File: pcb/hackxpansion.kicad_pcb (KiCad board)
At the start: 2 copper layers, 30 parts, among them J1 Conn_01x03_MountingPin, SW1 SW_Push, SW2 SW_Push, U1 ADS131M08xPBS, U2 RP2354B, Y1 ABM8-272-T3

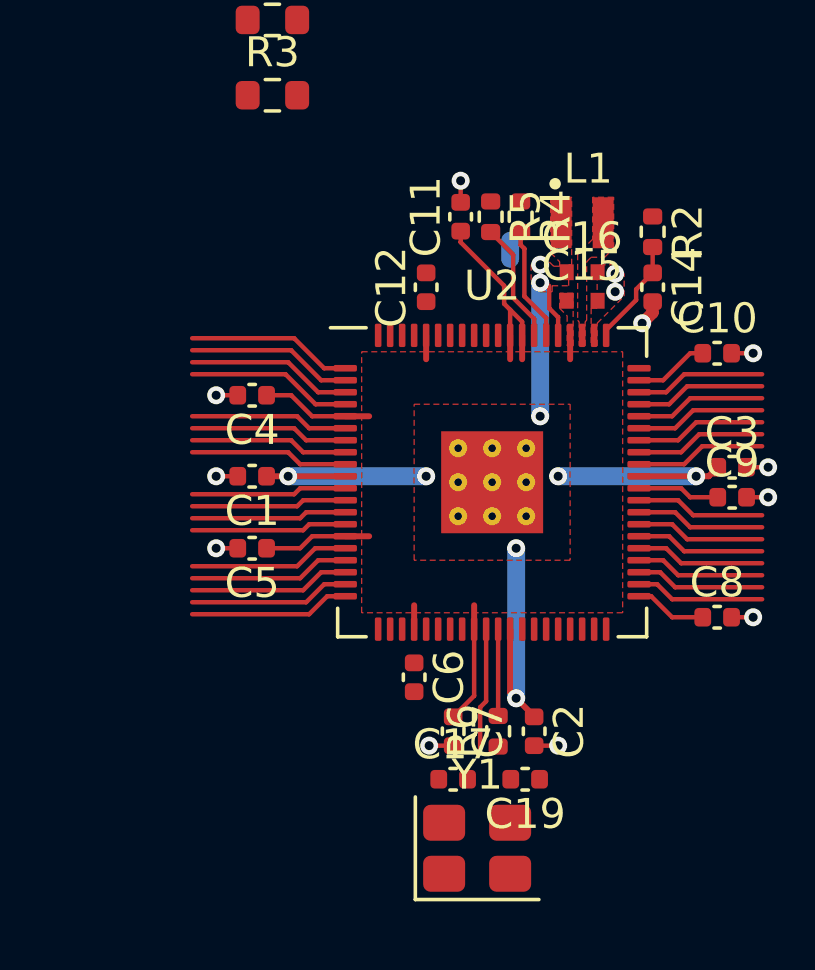
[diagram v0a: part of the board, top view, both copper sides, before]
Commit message: More fanout
Just a little bit further with the fanout of the RP2354B
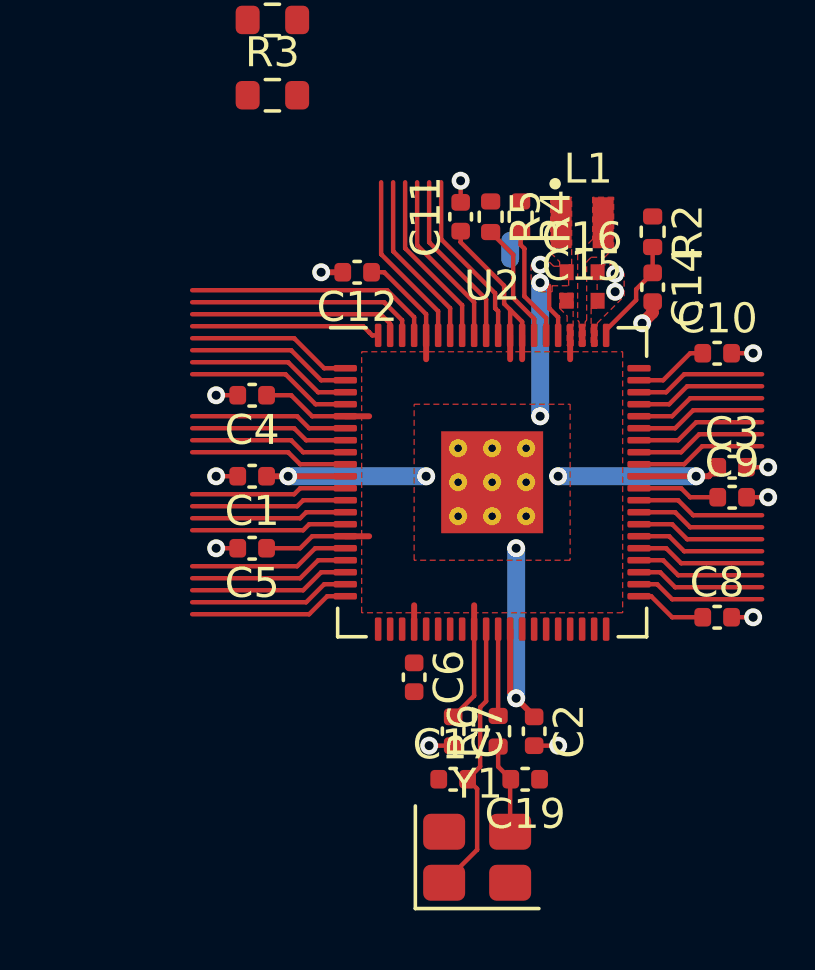
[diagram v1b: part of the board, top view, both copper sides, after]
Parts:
- moved C12 2.35 mm to (124.5, 78.0), turned to 180 degrees
- moved Y1 0.30 mm to (128.5, 97.5)
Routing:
- net /RP2354B/GPIO0: track 0.00 -> 8.38 mm
- net /RP2354B/GPIO1: track 0.00 -> 7.75 mm
- net /RP2354B/GPIO2: track 0.00 -> 7.12 mm
- net /RP2354B/GPIO3: track 0.00 -> 6.33 mm
- net /RP2354B/QSPI_SS: track 0.00 -> 5.89 mm
- net /RP2354B/QSPI_SD2: track 0.00 -> 5.89 mm
- net /RP2354B/QSPI_SD0: track 0.00 -> 5.89 mm
- net /RP2354B/QSPI_SCLK: track 0.00 -> 5.89 mm
- net /RP2354B/QSPI_SD3: track 0.00 -> 5.89 mm
- net /RP2354B/QSPI_SD1: track 0.00 -> 5.89 mm
- net Net-(U2-XIN): track 4.09 -> 9.30 mm
- net +3V3: track 28.1 -> 31.2 mm
- net Net-(C19-Pad2): track 0.00 -> 3.02 mm
- net GND: track 8.22 -> 8.94 mm, vias 13 -> 14

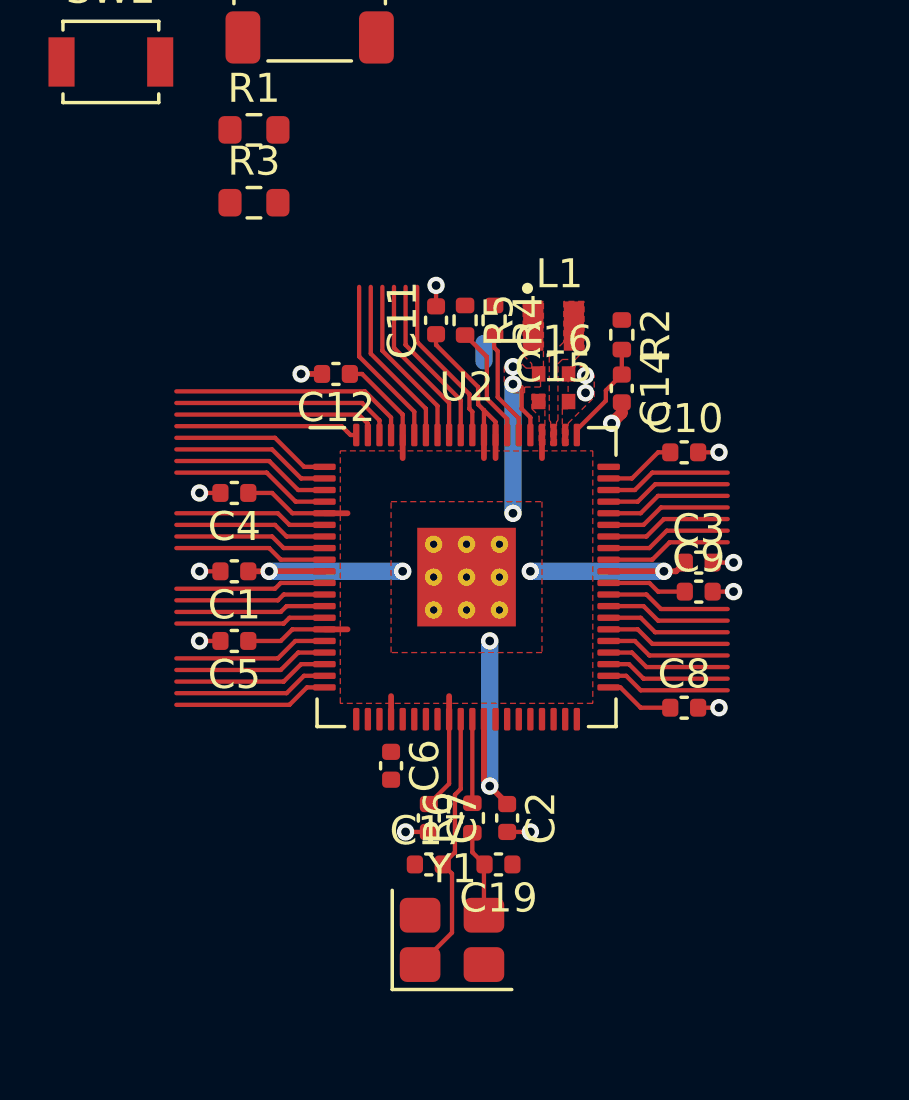
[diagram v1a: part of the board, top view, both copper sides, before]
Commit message: Completed fanout
Completed the fanout for the rp2354B also placed the silkscreen labels in places where you can read them.
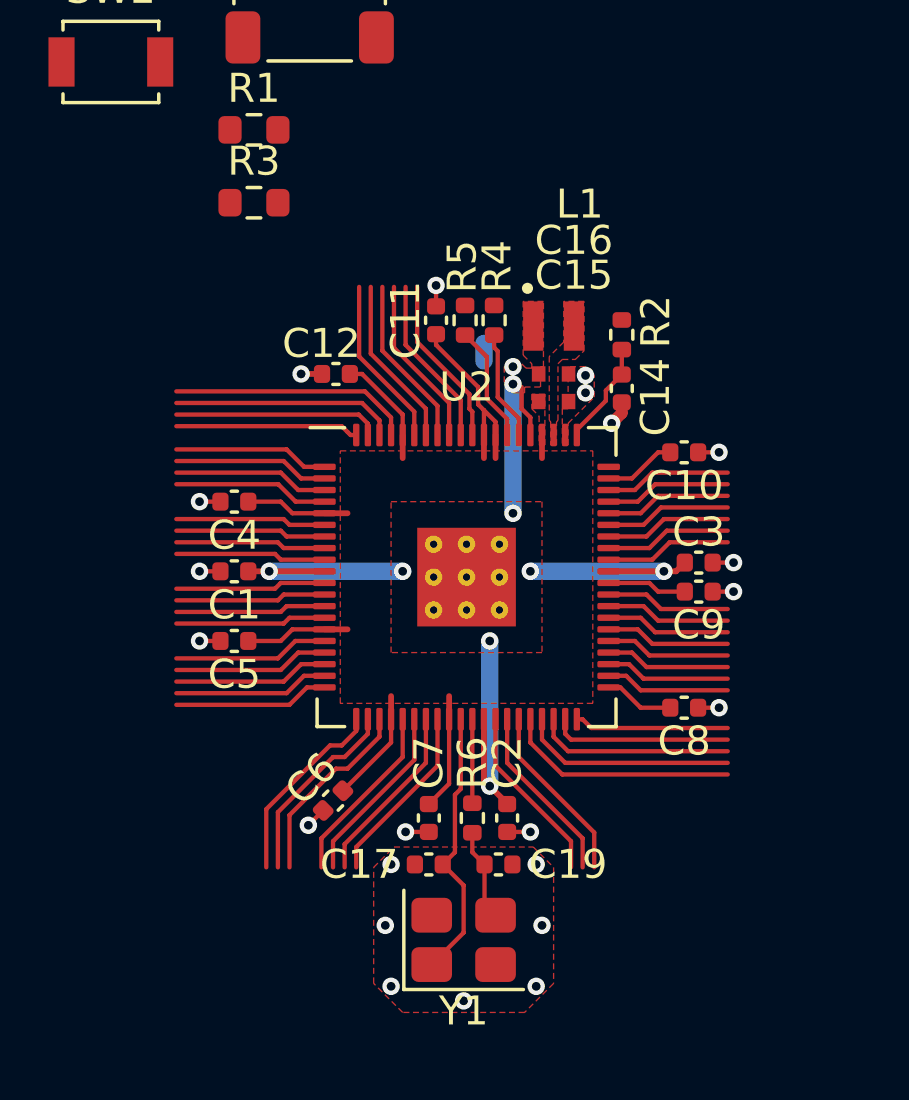
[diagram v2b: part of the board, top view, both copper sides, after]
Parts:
- moved C6 2.33 mm to (124.4, 92.7), turned to -135 degrees
- moved Y1 0.40 mm to (128.9, 97.5)
- moved C4 0.30 mm to (121.0, 82.4)
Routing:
- net /RP2354B/GPIO28: track 0.00 -> 8.06 mm
- net /RP2354B/GPIO29: track 0.00 -> 7.43 mm
- net /RP2354B/GPIO30: track 0.00 -> 6.81 mm
- net /RP2354B/GPIO21: track 0.00 -> 6.62 mm
- net /RP2354B/GPIO23: track 0.00 -> 6.62 mm
- net /RP2354B/GPIO22: track 0.00 -> 6.62 mm
- net /RP2354B/GPIO27: track 0.00 -> 6.26 mm
- net /RP2354B/GPIO26: track 0.00 -> 6.26 mm
- net /RP2354B/GPIO25: track 0.00 -> 6.26 mm
- net /RP2354B/GPIO24: track 0.00 -> 6.26 mm
- net /RP2354B/GPIO31: track 0.00 -> 6.19 mm
- net /RP2354B/SWDIO: track 0.00 -> 6.18 mm
- net /RP2354B/SWCLK: track 0.00 -> 6.18 mm
- net /RP2354B/RUN: track 0.00 -> 6.18 mm
- net /RP2354B/GPIO32: track 0.00 -> 5.33 mm
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
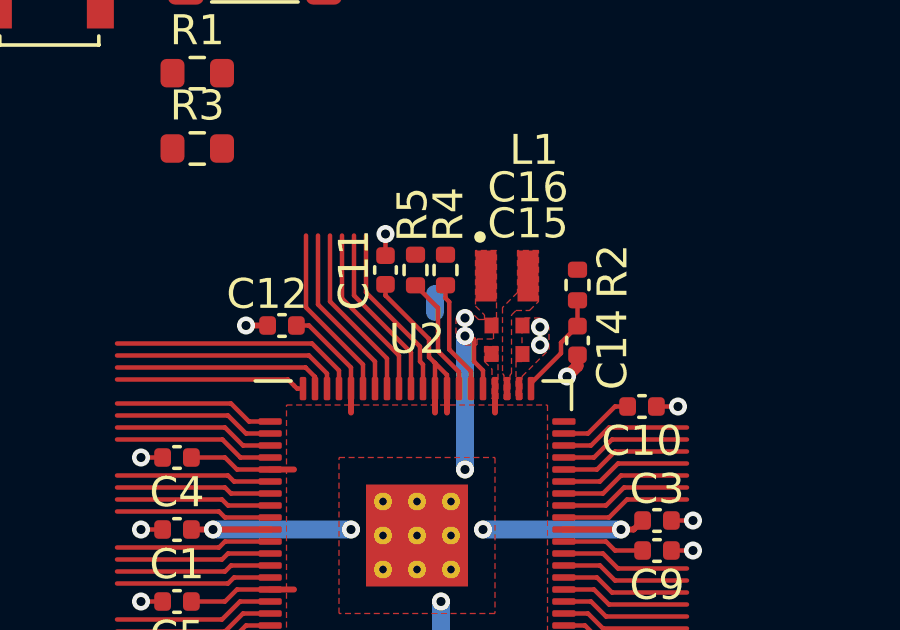
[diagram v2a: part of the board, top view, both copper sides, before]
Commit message: Fixed 1V1 trace and added a bit to ADC schematic
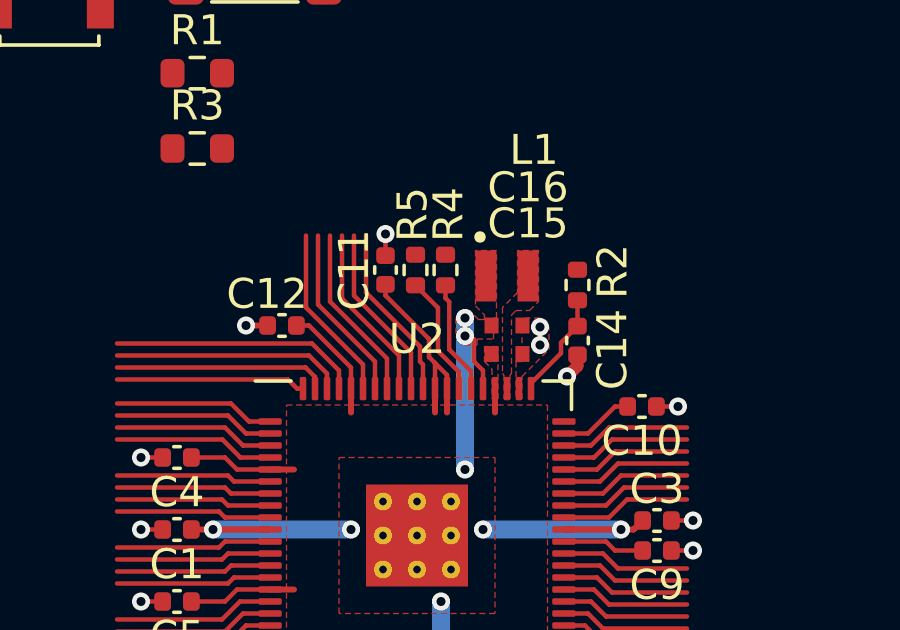
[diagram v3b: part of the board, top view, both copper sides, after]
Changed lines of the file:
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@@
-	)
-	(segment
-		(start 129.6 76.95)
-		(end 129.6 77.55)
-		(width 0.6)
-		(layer "B.Cu")
-		(net 31)
 	)
 	(segment
@@
 		(width 0.6)
 		(layer "B.Cu")
+		(net 31)
+	)
+	(segment
+		(start 130.6 78.35)
+		(end 130.6 77.75)
+		(width 0.6)
+		(layer "B.Cu")

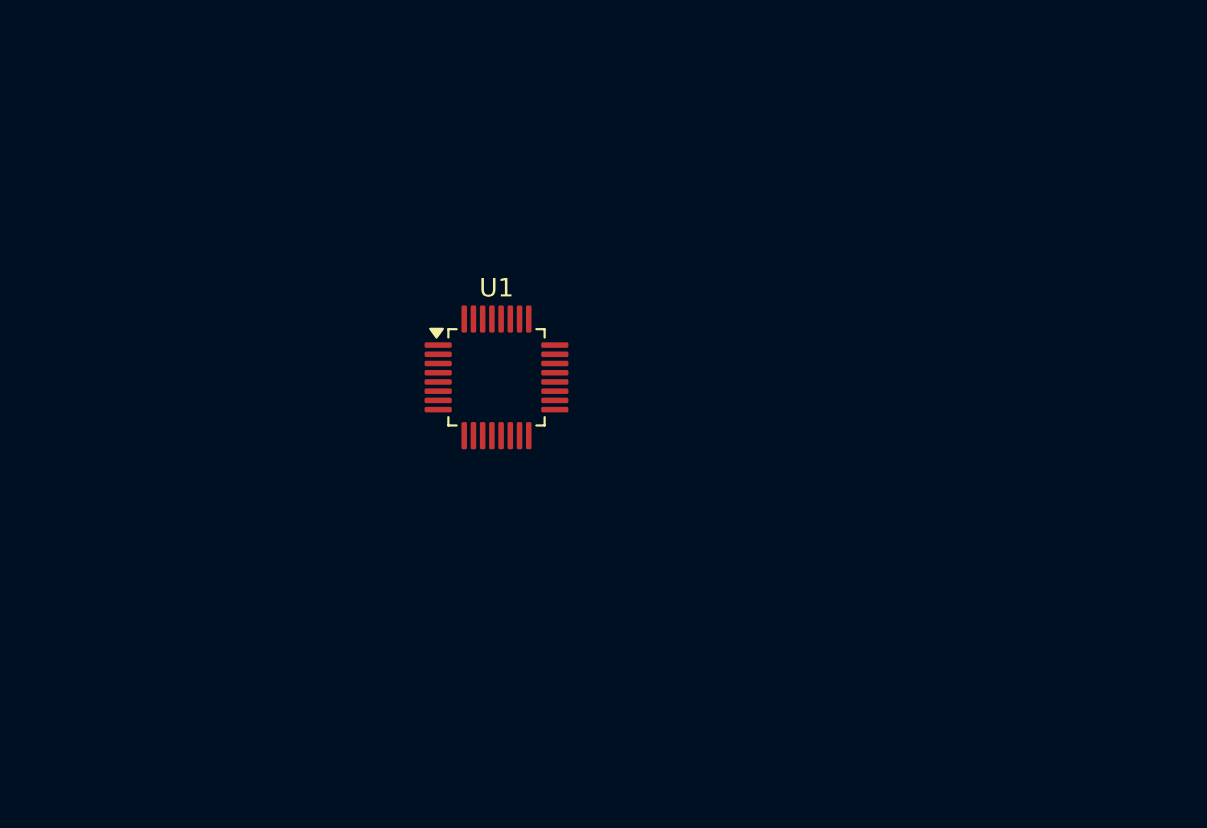
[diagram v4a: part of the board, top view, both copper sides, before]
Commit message: added new adc symbol
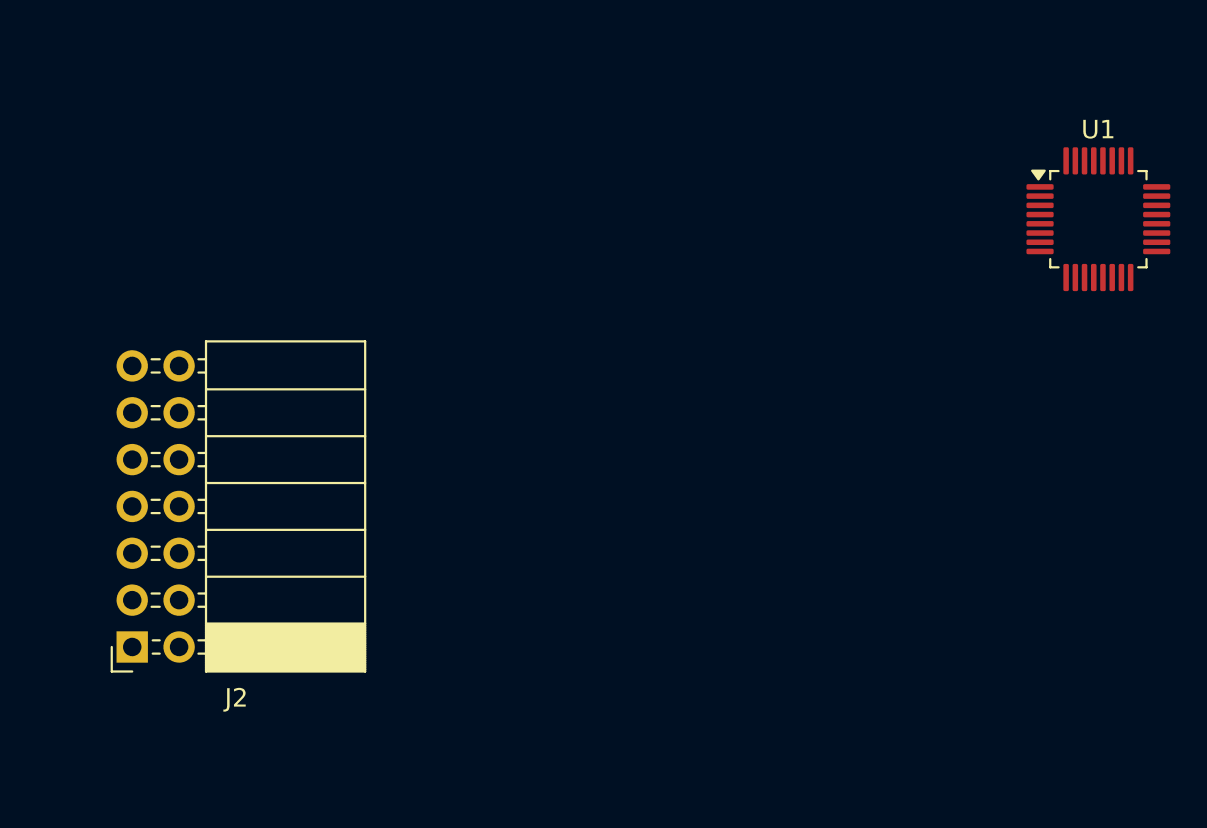
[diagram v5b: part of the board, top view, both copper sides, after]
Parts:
- added J2: Conn_02x07_Counter_Clockwise, Connector_PinSocket_2.54mm:PinSocket_2x07_P2.54mm_Horizontal, F.Cu at (146.8, 92.6)
- moved U1 33.7 mm to (199.1, 69.4)
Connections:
- U1 pad 13: Net-(U1-AGND-Pad13) -> GND
- U1 pad 14: unconnected-(U1-REFIN-Pad14) -> +3V3
- U1 pad 15: unconnected-(U1-AVDD-Pad15) -> +3V3
- U1 pad 16: unconnected-(U1-~{SYNC}/~{RESET}-Pad16) -> /ADC/~{RESET}
- U1 pad 17: unconnected-(U1-~{CS}-Pad17) -> /ADC/CS
- U1 pad 18: unconnected-(U1-~{DRDY}-Pad18) -> /ADC/~{DRDY}
- U1 pad 19: unconnected-(U1-SCLK-Pad19) -> /ADC/SCLK
- U1 pad 20: unconnected-(U1-DOUT-Pad20) -> /ADC/MISO
- U1 pad 21: unconnected-(U1-DIN-Pad21) -> /ADC/MOSI
- U1 pad 23: unconnected-(U1-XTAL1/CLKIN-Pad23) -> /ADC/CLKIN
- U1 pad 24: unconnected-(U1-CAP-Pad24) -> Net-(U1-CAP)
- U1 pad 25: unconnected-(U1-DGND-Pad25) -> GND
- U1 pad 26: unconnected-(U1-DVDD-Pad26) -> +3V3
- U1 pad 27: Net-(U1-AGND-Pad13) -> GND
- U1 pad 28: Net-(U1-AGND-Pad13) -> GND
- U1 pad 29: unconnected-(U1-AIN0P-Pad29) -> Net-(U1-AIN0P)
- U1 pad 30: unconnected-(U1-AIN0N-Pad30) -> Net-(U1-AIN0N)

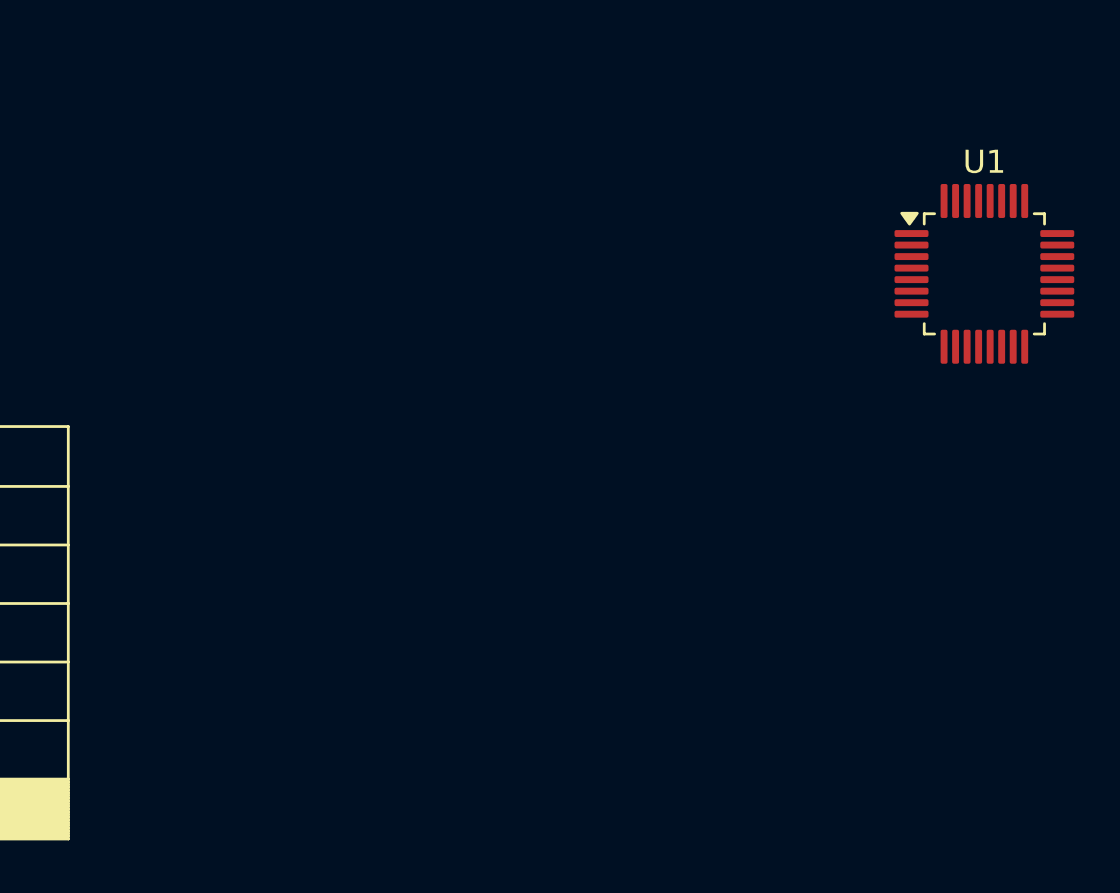
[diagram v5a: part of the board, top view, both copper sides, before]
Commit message: finished adding new adc, and started on dispaly
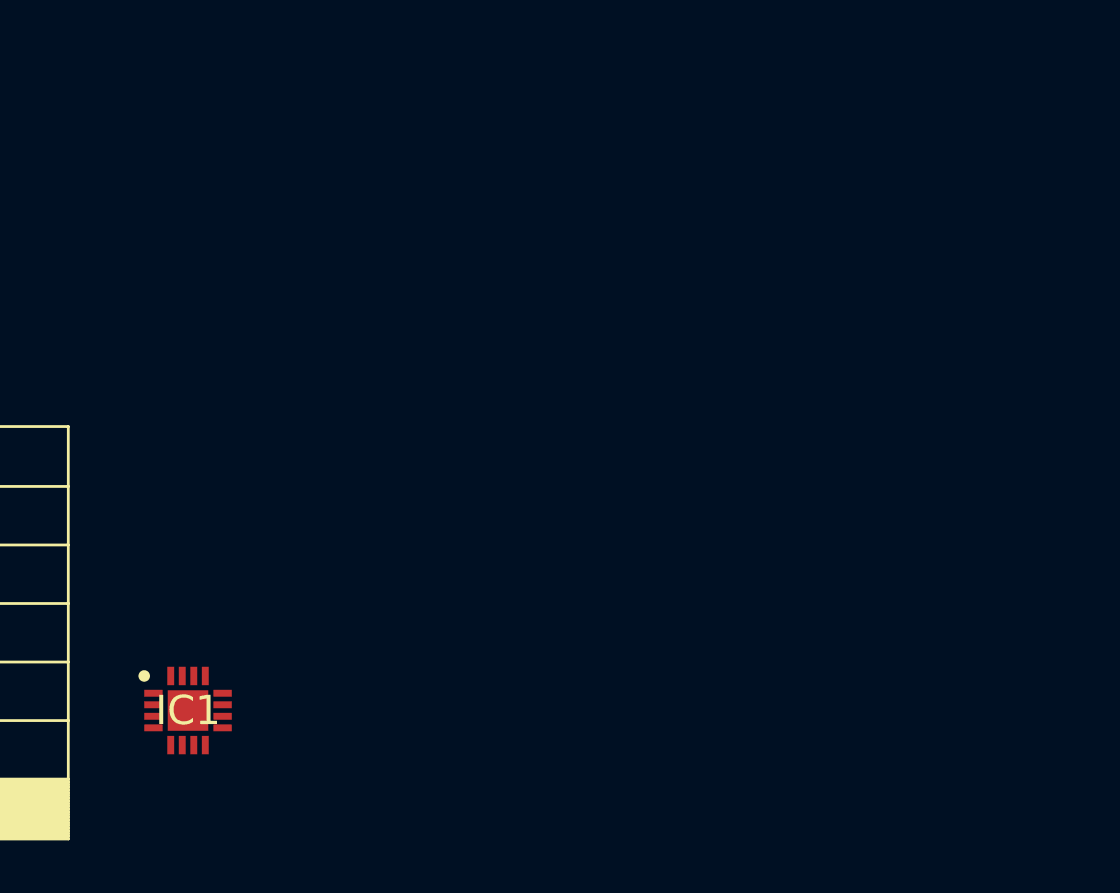
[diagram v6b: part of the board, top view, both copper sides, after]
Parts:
- removed U1: ADS131M08xPBS, Package_QFP:TQFP-32_5x5mm_P0.5mm
- added IC1: ADS7128IRTET, ADS7128IRTET:QFN50P300X300X80-17N-D, F.Cu at (164.6, 88.4)

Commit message: STARTED WORKING ON SYMBOL
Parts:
- removed J2: Conn_02x07_Counter_Clockwise, Connector_PinSocket_2.54mm:PinSocket_2x07_P2.54mm_Horizontal
- added J3: Conn_02x07_Counter_Clockwise, Connector_PinSocket_2.54mm:PinSocket_2x07_P2.54mm_Horizontal, F.Cu at (197.1, 103.8)
- added J4: Conn_02x07_Counter_Clockwise, Connector_PinSocket_2.54mm:PinSocket_2x07_P2.54mm_Horizontal, F.Cu at (197.1, 125.6)
- added J5: Conn_02x07_Counter_Clockwise, Connector_PinSocket_2.54mm:PinSocket_2x07_P2.54mm_Horizontal, F.Cu at (215.0, 125.6)
- added J6: Conn_02x07_Counter_Clockwise, Connector_PinSocket_2.54mm:PinSocket_2x07_P2.54mm_Horizontal, F.Cu at (215.0, 103.8)
- added Q1: SS8050, Package_TO_SOT_THT:TO-92, F.Cu at (221.3, 126.6)
